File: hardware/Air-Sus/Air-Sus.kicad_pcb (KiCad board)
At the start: 2 copper layers, 50.1 x 63.6 mm, 54 parts, among them IC1 ABPMRRV060MG2A3, IC3 ABPMRRV060MG2A3, J1 53307-2471, J2 Conn_01x05, J4 MX150_02x06_Vertical, J5 Conn_01x06, U1 Opamp_Dual, U2 LDO40LPURY

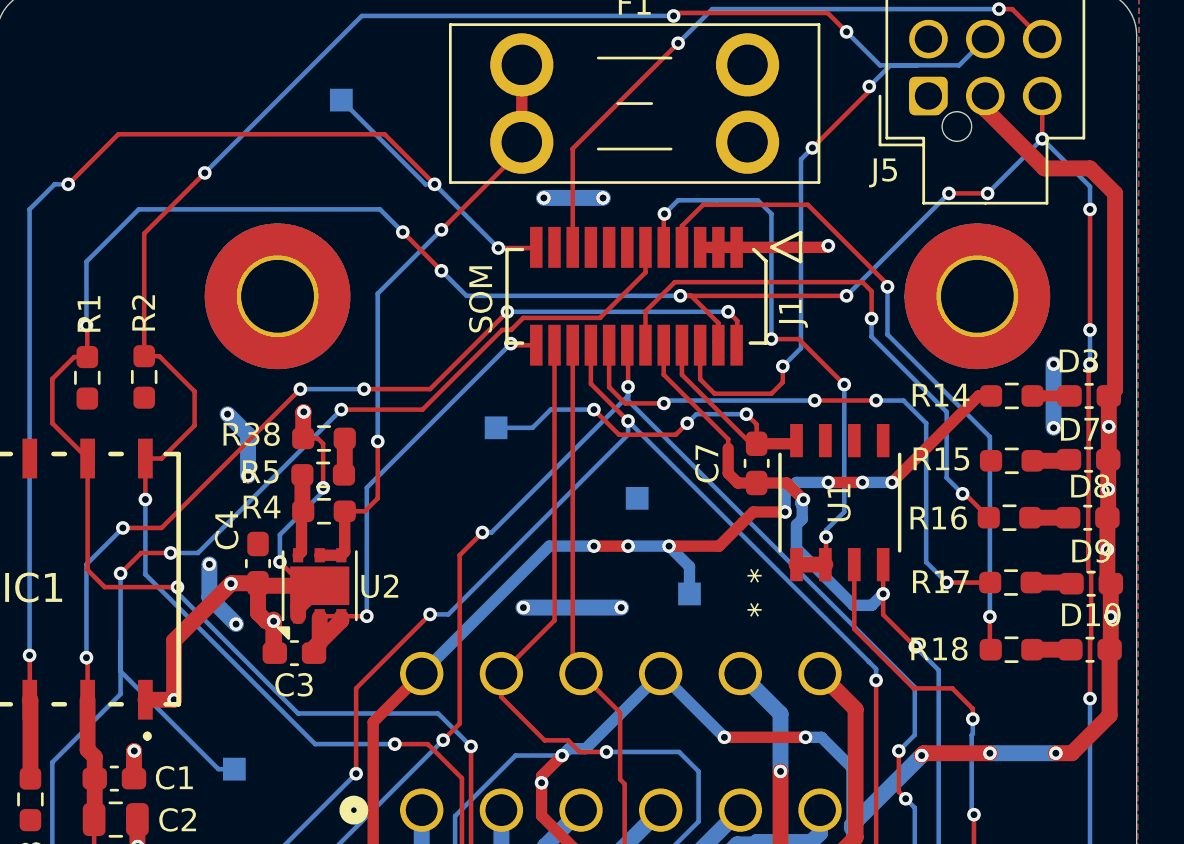
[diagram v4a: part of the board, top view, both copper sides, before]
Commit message: fixed ir-board sensor
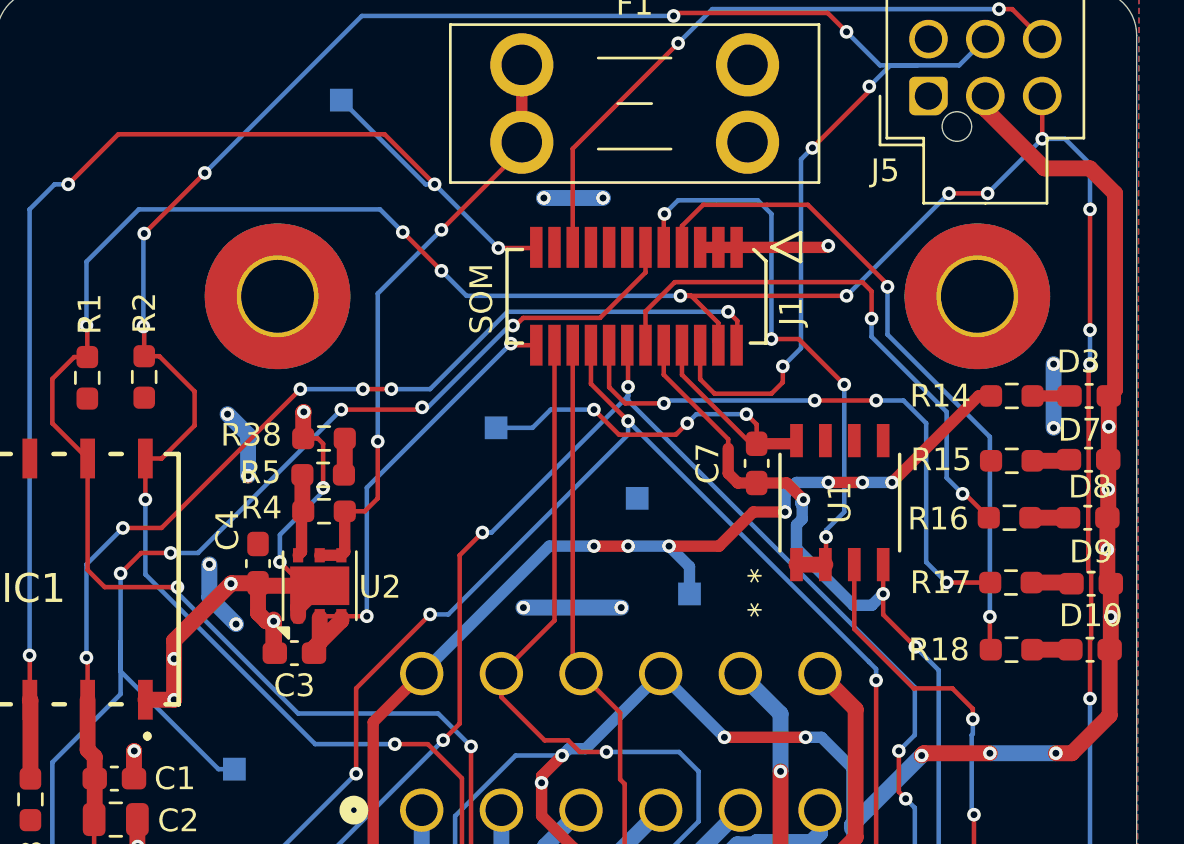
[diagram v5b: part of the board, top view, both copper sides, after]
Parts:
- moved G*** 0.70 mm to (100.6, 36.8)
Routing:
- net /SDA: track 139.8 -> 140.4 mm
- net /pressure_err2: track 73.7 -> 74.0 mm, vias 4 -> 6
- net /SCL: track 134.9 -> 135.0 mm, vias 12 -> 14
- net GND: vias 30 -> 31
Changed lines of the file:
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@@
 	(footprint "UTSVT_Logos:LHRs_LOGO"
 		(layer "F.Cu")
-		(at 100.6 37.5)
+		(at 100.569845 36.79961)
 		(property "Reference" "G***"
 			(at 2.286 8.128 0)
@@
 	)
 	(segment
+		(start 98.95 62.65)
+		(end 98.95 61.85)
+		(width 0.7)
+		(layer "F.Cu")
+		(net 3)
+	)
+	(segment
 		(start 97.515 89.6375)
 		(end 97.515 87.835)
@@
 	(segment
 		(start 98.95 64.45)
-		(end 98.95 61.85)
+		(end 98.95 62.65)
 		(width 0.7)
 		(layer "F.Cu")
@@
 	)
 	(via
+		(at 98.95 62.65)
+		(size 0.6)
+		(drill 0.3)
+		(layers "F.Cu" "B.Cu")
+		(net 3)
+	)
+	(via
 		(at 140 55.2)
 		(size 0.6)
@@
 	)
 	(segment
-		(start 139.2 41.9)
-		(end 137.1 39.8)
-		(width 0.2)
-		(layer "B.Cu")
-		(net 13)
-	)
-	(segment
 		(start 133 42.2)
 		(end 128.5 46.7)
@@
 	)
 	(segment
+		(start 139.2 42.9)
+		(end 139.2 40.9)
+		(width 0.2)
+		(layer "B.Cu")
+		(net 13)
+	)
+	(segment
 		(start 108 42.9)
 		(end 109 43.9)
@@
 	)
 	(segment
+		(start 139.2 40.9)
+		(end 138.1 39.8)
+		(width 0.2)
+		(layer "B.Cu")
+		(net 13)
+	)
+	(segment
 		(start 137.1 39.8)
 		(end 134.7 42.2)
@@
 	)
 	(segment
-		(start 139.2 41.9)
-		(end 139.2 42.9)
+		(start 138.1 39.8)
+		(end 137.1 39.8)
 		(width 0.2)
 		(layer "B.Cu")
@@
 	)
 	(segment
-		(start 97.6375 49.3525)
-		(end 97.6375 43.9625)
-		(width 0.2)
-		(layer "F.Cu")
-		(net 14)
-	)
-	(segment
 		(start 128.35 75.9)
 		(end 128.425 75.975)
@@
 	)
 	(segment
+		(start 97.6375 48.0875)
+		(end 97.6 48.05)
+		(width 0.2)
+		(layer "F.Cu")
+		(net 14)
+	)
+	(segment
 		(start 113.955 73.755)
 		(end 111.6 71.4)
@@
 	)
 	(segment
+		(start 97.6375 49.3525)
+		(end 97.6375 48.0875)
+		(width 0.2)
+		(layer "F.Cu")
+		(net 14)
+	)
+	(segment
 		(start 128.425 75.975)
 		(end 128.425 76.001)
@@
 	)
 	(via
+		(at 97.6375 43.9625)
+		(size 0.6)
+		(drill 0.3)
+		(layers "F.Cu" "B.Cu")
+		(net 14)
+	)
+	(via
 		(at 120.9 34.4)
 		(size 0.6)
@@
 	)
 	(via
+		(at 97.6 48.05)
+		(size 0.6)
+		(drill 0.3)
+		(layers "F.Cu" "B.Cu")
+		(net 14)
+	)
+	(via
 		(at 125.7 49.8)
 		(size 0.6)
@@
 	)
 	(segment
+		(start 97.6 44)
+		(end 97.6375 43.9625)
+		(width 0.2)
+		(layer "B.Cu")
+		(net 14)
+	)
+	(segment
 		(start 119.247918 76)
 		(end 119.349999 75.897919)
@@
 	)
 	(segment
+		(start 97.6 48.05)
+		(end 97.6 44)
+		(width 0.2)
+		(layer "B.Cu")
+		(net 14)
+	)
+	(segment
 		(start 129.971 36.571)
 		(end 131.6 36.571)
@@
 	)
 	(segment
+		(start 109.8671 51.6171)
+		(end 109.85 51.6)
+		(width 0.2)
+		(layer "F.Cu")
+		(net 17)
+	)
+	(segment
 		(start 109.8671 51.7)
 		(end 106.3 51.7)
@@
 	)
 	(segment
-		(start 113.7615 48.199)
-		(end 113.3681 48.199)
+		(start 109.8671 51.7)
+		(end 109.8671 51.6171)
 		(width 0.2)
 		(layer "F.Cu")
@@
 	)
 	(segment
-		(start 113.3681 48.199)
-		(end 109.8671 51.7)
-		(width 0.2)
-		(layer "F.Cu")
-		(net 17)
-	)
-	(segment
 		(start 117.668503 47.669)
 		(end 114.2915 47.669)
@@
 	)
 	(via
+		(at 113.843094 48.005436)
+		(size 0.6)
+		(drill 0.3)
+		(layers "F.Cu" "B.Cu")
+		(net 17)
+	)
+	(via
 		(at 93.1 81.1)
 		(size 0.6)
@@
 		(net 17)
 	)
+	(via
+		(at 109.85 51.6)
+		(size 0.6)
+		(drill 0.3)
+		(layers "F.Cu" "B.Cu")
+		(net 17)
+	)
 	(segment
 		(start 93.6 80.6)
@@
 	)
 	(segment
+		(start 110.1 51.6)
+		(end 113.694564 48.005436)
+		(width 0.2)
+		(layer "B.Cu")
+		(net 17)
+	)
+	(segment
+		(start 109.85 51.6)
+		(end 110.1 51.6)
+		(width 0.2)
+		(layer "B.Cu")
+		(net 17)
+	)
+	(segment
 		(start 96.6 61.9)
 		(end 96.6 58.9)
@@
 	)
 	(segment
+		(start 113.694564 48.005436)
+		(end 113.843094 48.005436)
+		(width 0.2)
+		(layer "B.Cu")
+		(net 17)
+	)
+	(segment
 		(start 100 58)
 		(end 98.8 58)
@@
 	)
 	(segment
-		(start 107.3 50.8)
-		(end 110.2 50.8)
-		(width 0.2)
-		(layer "F.Cu")
-		(net 22)
-	)
-	(segment
 		(start 95.1 89.5125)
 		(end 94.975 89.6375)
@@
 	)
 	(segment
-		(start 110.2 50.8)
-		(end 113.6 47.4)
-		(width 0.2)
-		(layer "F.Cu")
-		(net 22)
-	)
-	(segment
 		(start 123.3 47.4)
 		(end 123.7 47.8)
@@
 	)
 	(segment
+		(start 107.25 50.8)
+		(end 108.5 50.8)
+		(width 0.2)
+		(layer "F.Cu")
+		(net 22)
+	)
+	(segment
 		(start 95.4625 67.915)
 		(end 95.4625 69.69)
@@
 	)
 	(via
-		(at 107.3 50.8)
+		(at 95.1 87.8)
 		(size 0.6)
 		(drill 0.3)
@@
 	)
 	(via
-		(at 95.1 87.8)
+		(at 96.7 56.9)
 		(size 0.6)
 		(drill 0.3)
@@
 	)
 	(via
-		(at 96.7 56.9)
+		(at 95.1 62.6)
 		(size 0.6)
 		(drill 0.3)
@@
 	)
 	(via
-		(at 95.1 62.6)
+		(at 107.25 50.8)
 		(size 0.6)
 		(drill 0.3)
@@
 	)
 	(via
-		(at 113.6 47.4)
+		(at 96.2 74)
 		(size 0.6)
 		(drill 0.3)
@@
 	)
 	(via
-		(at 96.2 74)
+		(at 108.5 50.8)
 		(size 0.6)
 		(drill 0.3)
@@
 	)
 	(segment
+		(start 107.3 50.8)
+		(end 107.25 50.8)
+		(width 0.2)
+		(layer "B.Cu")
+		(net 22)
+	)
+	(segment
 		(start 95.1 62.6)
 		(end 95.1 58.5)
@@
 	)
 	(segment
+		(start 110.2 50.8)
+		(end 113.6 47.4)
+		(width 0.2)
+		(layer "B.Cu")
+		(net 22)
+	)
+	(segment
 		(start 96.2 74)
 		(end 96.2 86.7)
@@
 		(width 0.2)
 		(layer "B.Cu")
+		(net 22)
+	)
+	(segment
+		(start 108.5 50.8)
+		(end 110.2 50.8)
+		(width 0.2)
+		(layer "B.Cu")

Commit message: finished irboard, tempboard
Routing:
- net +3.3V: track 45.4 -> 51.2 mm
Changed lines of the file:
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@@
 	)
 	(segment
+		(start 92.475 95)
+		(end 93.95 93.525)
+		(width 0.5)
+		(layer "F.Cu")
+		(net 1)
+	)
+	(segment
 		(start 96.6 78.075)
 		(end 96.6 79.8)
@@
 	)
 	(segment
+		(start 119.83 73.12)
+		(end 121.4 71.55)
+		(width 0.7)
+		(layer "F.Cu")
+		(net 1)
+	)
+	(segment
 		(start 100.5 58.4)
 		(end 100.5 58.5)
@@
 	)
 	(segment
+		(start 93.95 93.525)
+		(end 93.95 93.5)
+		(width 0.5)
+		(layer "F.Cu")
+		(net 1)
+	)
+	(segment
 		(start 102.2 54.7)
 		(end 102.2 54.6)
@@
 	)
 	(segment
+		(start 119.83 74.5)
+		(end 119.83 73.12)
+		(width 0.7)
+		(layer "F.Cu")
+		(net 1)
+	)
+	(segment
 		(start 119.84 86.910057)
 		(end 117.6 89.150057)
@@
 		(start 106.3 60.78)
 		(end 105.35 60.78)
-		(width 0.2)
+		(width 0.5)
 		(layer "F.Cu")
 		(net 4)
@@
 	)
 	(segment
-		(start 118.75 78)
-		(end 118.75 75.450057)
+		(start 117.95 84)
+		(end 117.95 81.25)
 		(width 0.2)
 		(layer "F.Cu")
@@
 	)
 	(segment
-		(start 119.174 73.8411)
-		(end 118.75 73.4171)
+		(start 118.55 65.017099)
+		(end 116.8329 63.299999)
 		(width 0.2)
 		(layer "F.Cu")
@@
 	)
 	(segment
-		(start 117.95 84)
-		(end 117.95 81.25)
+		(start 118.75 75.450057)
+		(end 119.05 75.150057)
+		(width 0.2)
+		(layer "F.Cu")
+		(net 39)
+	)
+	(segment
+		(start 118.75 68.15)
+		(end 118.55 67.95)
+		(width 0.2)
+		(layer "F.Cu")
+		(net 39)
+	)
+	(segment
+		(start 118.75 73.4171)
+		(end 118.75 68.15)
 		(width 0.2)
 		(layer "F.Cu")
@@
 	)
 	(segment
-		(start 119.174 75.026057)
-		(end 119.174 73.8411)
-		(width 0.2)
-		(layer "F.Cu")
-		(net 39)
-	)
-	(segment
-		(start 118.55 65.017099)
-		(end 116.8329 63.299999)
+		(start 119.05 75.150057)
+		(end 119.05 73.7171)
 		(width 0.2)
 		(layer "F.Cu")
@@
 	)
 	(segment
-		(start 118.55 67.95)
-		(end 118.55 65.017099)
-		(width 0.2)
-		(layer "F.Cu")
-		(net 39)
-	)
-	(segment
-		(start 118.75 75.450057)
-		(end 119.174 75.026057)
-		(width 0.2)
-		(layer "F.Cu")
-		(net 39)
-	)
-	(segment
 		(start 117.95 81.25)
 		(end 118.5 80.7)
@@
 	)
 	(segment
-		(start 118.75 68.15)
-		(end 118.55 67.95)
+		(start 119.05 73.7171)
+		(end 118.75 73.4171)
 		(width 0.2)
 		(layer "F.Cu")
@@
 	)
 	(segment
-		(start 118.75 73.4171)
-		(end 118.75 68.15)
+		(start 118.55 67.95)
+		(end 118.55 65.017099)
 		(width 0.2)
 		(layer "F.Cu")
@@
 		(width 0.2)
 		(layer "F.Cu")
+		(net 39)
+	)
+	(segment
+		(start 118.75 78)
+		(end 118.75 75.450057)
+		(width 0.2)
+		(layer "F.Cu")
